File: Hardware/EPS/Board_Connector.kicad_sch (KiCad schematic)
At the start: 1 part

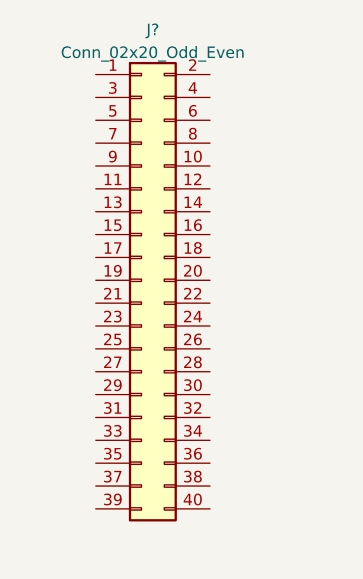
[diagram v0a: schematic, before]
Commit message: Added board connector layout
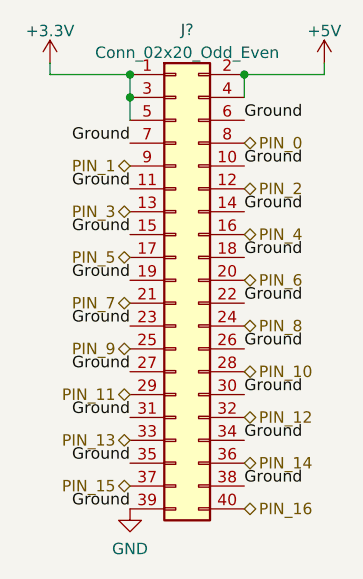
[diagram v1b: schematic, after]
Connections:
- net +3.3V: now reaches J?.1 (Pin_1)
- net +3.3V: now also J?.3 (Pin_3), J?.5 (Pin_5)
- net GND: now reaches J?.10 (Pin_10)
- net GND: now also J?.11 (Pin_11), J?.14 (Pin_14), J?.15 (Pin_15), J?.18 (Pin_18), J?.19 (Pin_19), J?.22 (Pin_22), J?.23 (Pin_23), J?.26 (Pin_26), J?.27 (Pin_27), J?.30 (Pin_30), J?.31 (Pin_31), J?.34 (Pin_34), J?.35 (Pin_35), J?.38 (Pin_38), J?.39 (Pin_39), J?.6 (Pin_6), J?.7 (Pin_7)
- net PIN_2: now reaches J?.12 (Pin_12)
- net PIN_3: now reaches J?.13 (Pin_13)
- net PIN_4: now reaches J?.16 (Pin_16)
- net PIN_5: now reaches J?.17 (Pin_17)
- net +5V: now reaches J?.2 (Pin_2)
- net +5V: now also J?.4 (Pin_4)
- net PIN_6: now reaches J?.20 (Pin_20)
- net PIN_7: now reaches J?.21 (Pin_21)
- net PIN_8: now reaches J?.24 (Pin_24)
- net PIN_9: now reaches J?.25 (Pin_25)
- net PIN_10: now reaches J?.28 (Pin_28)
- net PIN_11: now reaches J?.29 (Pin_29)
- net PIN_12: now reaches J?.32 (Pin_32)
- net PIN_13: now reaches J?.33 (Pin_33)
- net PIN_14: now reaches J?.36 (Pin_36)
- net PIN_15: now reaches J?.37 (Pin_37)
- net PIN_16: now reaches J?.40 (Pin_40)
- net PIN_0: now reaches J?.8 (Pin_8)
- net PIN_1: now reaches J?.9 (Pin_9)
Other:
- moved on the sheet: J?
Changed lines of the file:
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@@
 (kicad_sch (version 20211123) (generator eeschema)
   (paper "A4")
-  (symbol (lib_id "Connector_Generic:Conn_02x20_Odd_Even") (at 140.97 87.63 0) (unit 1)
-    (in_bom yes) (on_board yes) (fields_autoplaced)
-    (property "Reference" "J?" (id 0) (at 142.24 59.8002 0))
-    (property "Value" "Conn_02x20_Odd_Even" (id 1) (at 142.24 62.3371 0))
-    (property "Footprint" "" (id 2) (at 140.97 87.63 0)
-      (effects (font (size 1.27 1.27)) hide)
-    )
-    (property "Datasheet" "~" (id 3) (at 140.97 87.63 0)
+  (junction (at 152.4 64.77) (diameter 0) (color 0 0 0 0)
+  )
+  (junction (at 139.7 64.77) (diameter 0) (color 0 0 0 0)
+  )
+  (junction (at 139.7 67.31) (diameter 0) (color 0 0 0 0)
+  )
+  (wire (pts (xy 139.7 64.77) (xy 139.7 67.31))
+    (stroke (width 0) (type default) (color 0 0 0 0))
+  )
+  (wire (pts (xy 152.4 64.77) (xy 152.4 67.31))
+    (stroke (width 0) (type default) (color 0 0 0 0))
+  )
+  (wire (pts (xy 161.29 63.5) (xy 161.29 64.77))
+    (stroke (width 0) (type default) (color 0 0 0 0))
+  )
+  (wire (pts (xy 161.29 64.77) (xy 152.4 64.77))
+    (stroke (width 0) (type default) (color 0 0 0 0))
+  )
+  (wire (pts (xy 139.7 67.31) (xy 139.7 69.85))
+    (stroke (width 0) (type default) (color 0 0 0 0))
+  )
+  (wire (pts (xy 130.81 64.77) (xy 130.81 63.5))
+    (stroke (width 0) (type default) (color 0 0 0 0))
+  )
+  (wire (pts (xy 139.7 64.77) (xy 130.81 64.77))
+    (stroke (width 0) (type default) (color 0 0 0 0))
+  )
+  (label "Ground" (at 152.4 74.93 0)
+    (effects (font (size 1.27 1.27)) (justify left bottom))
+  )
+  (label "Ground" (at 152.4 80.01 0)
+    (effects (font (size 1.27 1.27)) (justify left bottom))
+  )
+  (label "Ground" (at 139.7 102.87 180)
+    (effects (font (size 1.27 1.27)) (justify right bottom))
+  )
+  (label "Ground" (at 139.7 87.63 180)
+    (effects (font (size 1.27 1.27)) (justify right bottom))
+  )
+  (label "Ground" (at 152.4 105.41 0)
+    (effects (font (size 1.27 1.27)) (justify left bottom))
+  )
+  (label "Ground" (at 139.7 113.03 180)
+    (effects (font (size 1.27 1.27)) (justify right bottom))
+  )
+  (label "Ground" (at 152.4 85.09 0)
+    (effects (font (size 1.27 1.27)) (justify left bottom))
+  )
+  (label "Ground" (at 152.4 90.17 0)
+    (effects (font (size 1.27 1.27)) (justify left bottom))
+  )
+  (label "Ground" (at 139.7 82.55 180)
+    (effects (font (size 1.27 1.27)) (justify right bottom))
+  )
+  (label "Ground" (at 139.7 92.71 180)
+    (effects (font (size 1.27 1.27)) (justify right bottom))
+  )
+  (label "Ground" (at 139.7 77.47 180)
+    (effects (font (size 1.27 1.27)) (justify right bottom))
+  )
+  (label "Ground" (at 139.7 107.95 180)
+    (effects (font (size 1.27 1.27)) (justify right bottom))
+  )
+  (label "Ground" (at 139.7 97.79 180)
+    (effects (font (size 1.27 1.27)) (justify right bottom))
+  )
+  (label "Ground" (at 152.4 100.33 0)
+    (effects (font (size 1.27 1.27)) (justify left bottom))
+  )
+  (label "Ground" (at 139.7 72.39 180)
+    (effects (font (size 1.27 1.27)) (justify right bottom))
+  )
+  (label "Ground" (at 152.4 69.85 0)
+    (effects (font (size 1.27 1.27)) (justify left bottom))
+  )
+  (label "Ground" (at 152.4 110.49 0)
+    (effects (font (size 1.27 1.27)) (justify left bottom))
+  )
+  (label "Ground" (at 152.4 95.25 0)
+    (effects (font (size 1.27 1.27)) (justify left bottom))
+  )
+  (hierarchical_label "PIN_9" (shape bidirectional) (at 139.7 95.25 180)
+    (effects (font (size 1.27 1.27)) (justify right))
+  )
+  (hierarchical_label "PIN_8" (shape bidirectional) (at 152.4 92.71 0)
+    (effects (font (size 1.27 1.27)) (justify left))
+  )
+  (hierarchical_label "PIN_5" (shape bidirectional) (at 139.7 85.09 180)
+    (effects (font (size 1.27 1.27)) (justify right))
+  )
+  (hierarchical_label "PIN_2" (shape bidirectional) (at 152.4 77.47 0)
+    (effects (font (size 1.27 1.27)) (justify left))
+  )
+  (hierarchical_label "PIN_12" (shape bidirectional) (at 152.4 102.87 0)
+    (effects (font (size 1.27 1.27)) (justify left))
+  )
+  (hierarchical_label "PIN_3" (shape bidirectional) (at 139.7 80.01 180)
+    (effects (font (size 1.27 1.27)) (justify right))
+  )
+  (hierarchical_label "PIN_10" (shape bidirectional) (at 152.4 97.79 0)
+    (effects (font (size 1.27 1.27)) (justify left))
+  )
+  (hierarchical_label "PIN_11" (shape bidirectional) (at 139.7 100.33 180)
+    (effects (font (size 1.27 1.27)) (justify right))
+  )
+  (hierarchical_label "PIN_13" (shape bidirectional) (at 139.7 105.41 180)
+    (effects (font (size 1.27 1.27)) (justify right))
+  )
+  (hierarchical_label "PIN_16" (shape bidirectional) (at 152.4 113.03 0)
+    (effects (font (size 1.27 1.27)) (justify left))
+  )
+  (hierarchical_label "PIN_4" (shape bidirectional) (at 152.4 82.55 0)
+    (effects (font (size 1.27 1.27)) (justify left))
+  )
+  (hierarchical_label "PIN_1" (shape bidirectional) (at 139.7 74.93 180)
+    (effects (font (size 1.27 1.27)) (justify right))
+  )
+  (hierarchical_label "PIN_6" (shape bidirectional) (at 152.4 87.63 0)
+    (effects (font (size 1.27 1.27)) (justify left))
+  )
+  (hierarchical_label "PIN_14" (shape bidirectional) (at 152.4 107.95 0)
+    (effects (font (size 1.27 1.27)) (justify left))
+  )
+  (hierarchical_label "PIN_15" (shape bidirectional) (at 139.7 110.49 180)
+    (effects (font (size 1.27 1.27)) (justify right))
+  )
+  (hierarchical_label "PIN_7" (shape bidirectional) (at 139.7 90.17 180)
+    (effects (font (size 1.27 1.27)) (justify right))
+  )
+  (hierarchical_label "PIN_0" (shape bidirectional) (at 152.4 72.39 0)
+    (effects (font (size 1.27 1.27)) (justify left))
+  )
+  (symbol (lib_id "Connector_Generic:Conn_02x20_Odd_Even") (at 144.78 87.63 0) (unit 1)
+    (in_bom yes) (on_board yes) (fields_autoplaced)
+    (property "Reference" "J?" (id 0) (at 146.05 59.8002 0))
+    (property "Value" "Conn_02x20_Odd_Even" (id 1) (at 146.05 62.3371 0))
+    (property "Footprint" "" (id 2) (at 144.78 87.63 0)
+      (effects (font (size 1.27 1.27)) hide)
+    )
+    (property "Datasheet" "~" (id 3) (at 144.78 87.63 0)
       (effects (font (size 1.27 1.27)) hide)
     )
@@
     (pin "9")
   )
+  (symbol (lib_id "power:+5V") (at 161.29 63.5 0) (unit 1)
+    (in_bom yes) (on_board yes) (fields_autoplaced)
+    (property "Reference" "#PWR?" (id 0) (at 161.29 67.31 0)
+      (effects (font (size 1.27 1.27)) hide)
+    )
+    (property "Value" "+5V" (id 1) (at 161.29 59.9242 0))
+    (property "Footprint" "" (id 2) (at 161.29 63.5 0)
+      (effects (font (size 1.27 1.27)) hide)
+    )
+    (property "Datasheet" "" (id 3) (at 161.29 63.5 0)
+      (effects (font (size 1.27 1.27)) hide)
+    )
+    (pin "1")
+  )
+  (symbol (lib_id "power:+3.3V") (at 130.81 63.5 0) (unit 1)
+    (in_bom yes) (on_board yes) (fields_autoplaced)
+    (property "Reference" "#PWR?" (id 0) (at 130.81 67.31 0)
+      (effects (font (size 1.27 1.27)) hide)
+    )
+    (property "Value" "+3.3V" (id 1) (at 130.81 59.9242 0))
+    (property "Footprint" "" (id 2) (at 130.81 63.5 0)
+      (effects (font (size 1.27 1.27)) hide)
+    )
+    (property "Datasheet" "" (id 3) (at 130.81 63.5 0)
+      (effects (font (size 1.27 1.27)) hide)
+    )
+    (pin "1")
+  )
+  (symbol (lib_id "power:GND") (at 139.7 113.03 0) (unit 1)
+    (in_bom yes) (on_board yes) (fields_autoplaced)
+    (property "Reference" "#PWR?" (id 0) (at 139.7 119.38 0)
+      (effects (font (size 1.27 1.27)) hide)
+    )
+    (property "Value" "GND" (id 1) (at 139.7 117.4734 0))
+    (property "Footprint" "" (id 2) (at 139.7 113.03 0)
+      (effects (font (size 1.27 1.27)) hide)
+    )
+    (property "Datasheet" "" (id 3) (at 139.7 113.03 0)
+      (effects (font (size 1.27 1.27)) hide)
+    )
+    (pin "1")
+  )
 )

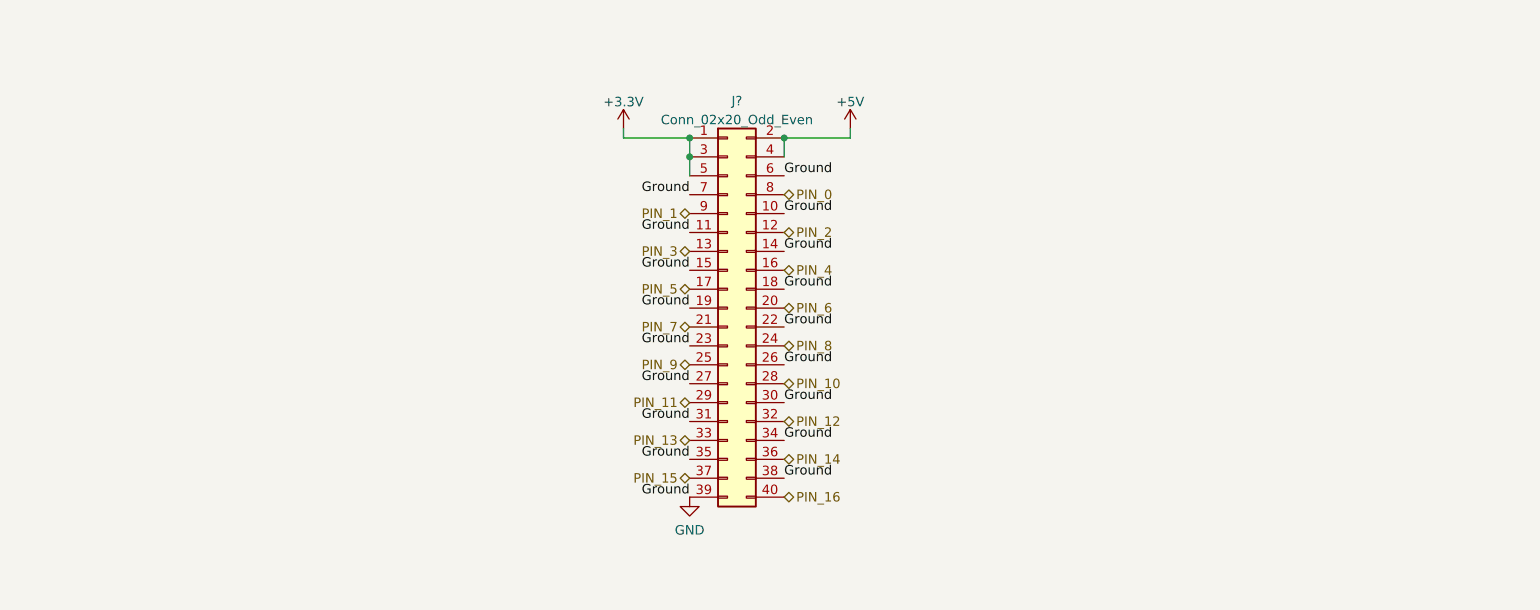
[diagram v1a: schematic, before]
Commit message: Fuse, Power Switch to 3.3V, connector ESD Prot.
v0.0.2
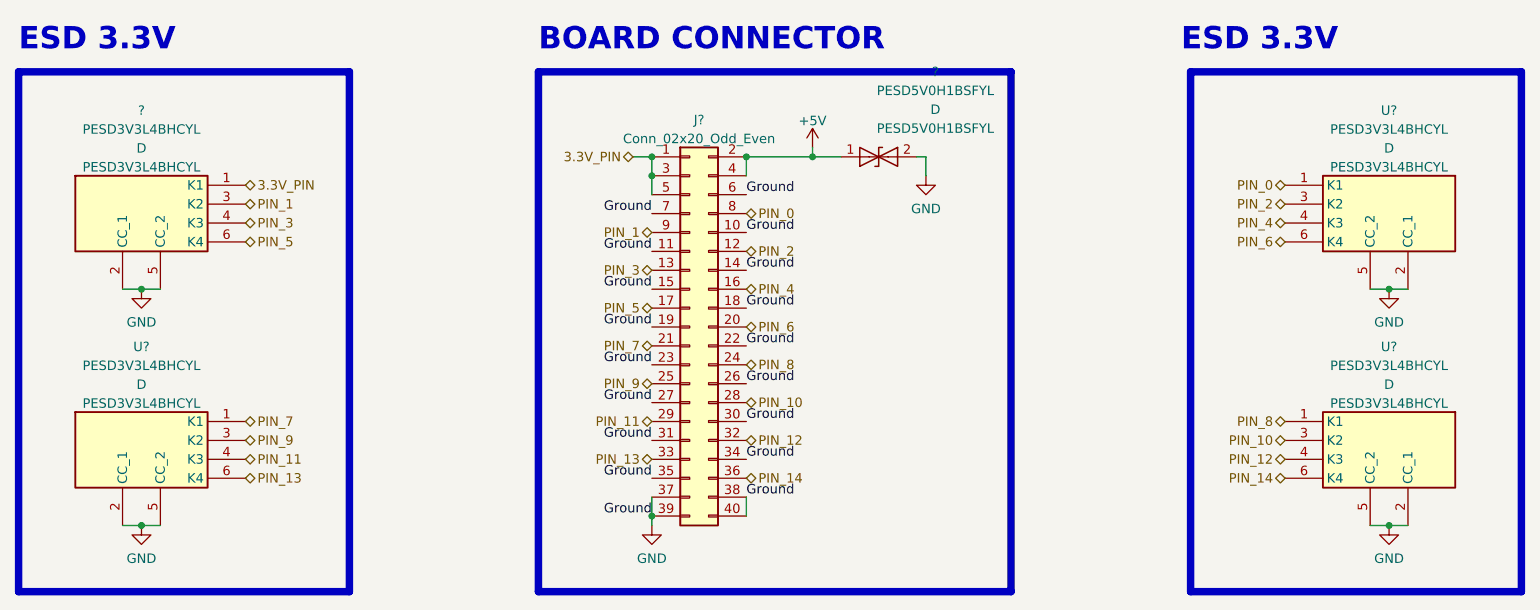
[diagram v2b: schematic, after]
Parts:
- added ?: PESD5V0H1BSFYL, symbol PESD5V0H1BSFYL:PESD5V0H1BSFYL
- added ?, U? (x3): PESD3V3L4BHCYL, symbol PESD3V3L4BHCYL:PESD3V3L4BHCYL
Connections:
- net PIN_15 is gone; now on net GND: J?.37 (Pin_37)
- net PIN_16 is gone; now on net GND: J?.40 (Pin_40)
- net +5V: now also ?.1 (A1)
- net GND: now also ?.2 (A2), ?.2 (CC_1), ?.5 (CC_2), U?.2 (CC_1), U?.2 (CC_1), U?.2 (CC_1), U?.5 (CC_2), U?.5 (CC_2), U?.5 (CC_2)
- net PIN_0: now also U?.1 (K1)
- net PIN_1: now also ?.3 (K2)
- net PIN_10: now also U?.3 (K2)
- net PIN_11: now also U?.4 (K3)
- net PIN_12: now also U?.4 (K3)
- net PIN_13: now also U?.6 (K4)
- net PIN_14: now also U?.6 (K4)
- net PIN_2: now also U?.3 (K2)
- net PIN_3: now also ?.4 (K3)
- net PIN_4: now also U?.4 (K3)
- net PIN_5: now also ?.6 (K4)
- net PIN_6: now also U?.6 (K4)
- net PIN_7: now also U?.1 (K1)
- net PIN_8: now also U?.1 (K1)
- net PIN_9: now also U?.3 (K2)
- net +3.3V renamed 3.3V_PIN
- net 3.3V_PIN: now also ?.1 (K1)
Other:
- note added: "BOARD CONNECTOR"
- note added: "ESD 3.3V"
- title: (none) -> EPS Schematics
- moved on the sheet: J?

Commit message: Defined pinout for board connector, major revision
v0.0.3 - Fixed erratas and cleaned the schematic
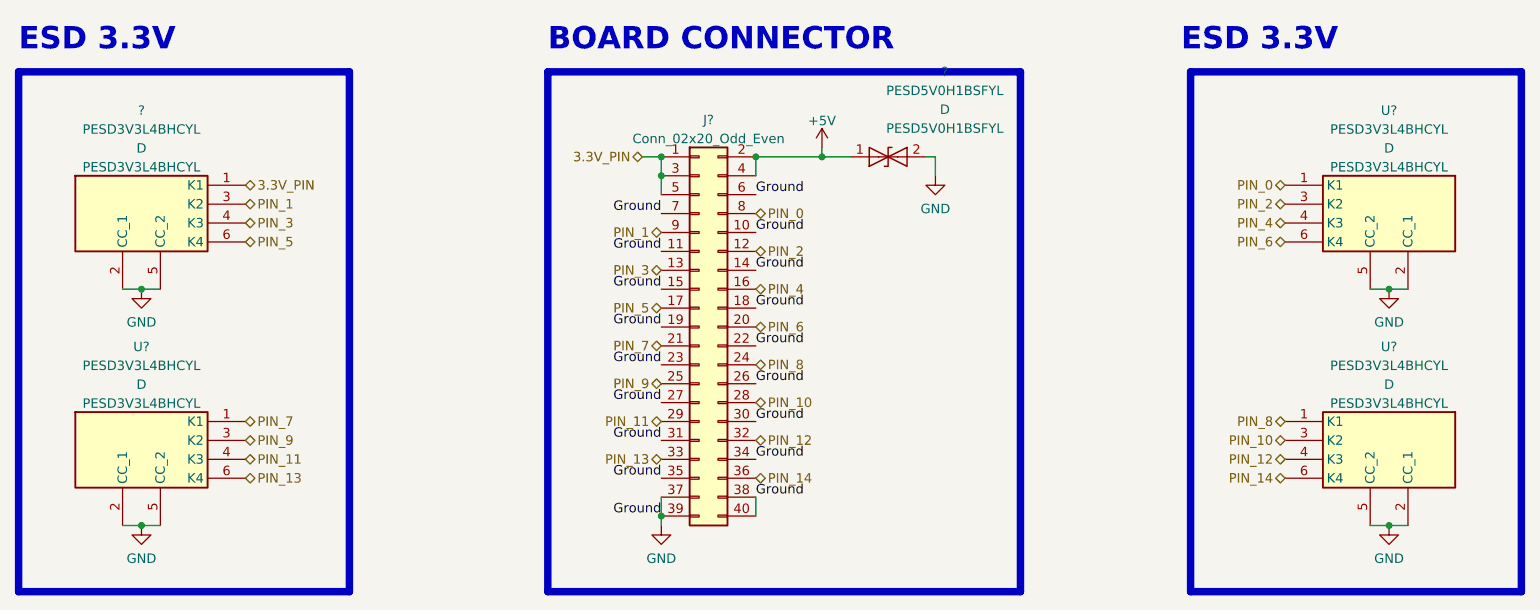
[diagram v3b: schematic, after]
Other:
- moved on the sheet: ?, J?
